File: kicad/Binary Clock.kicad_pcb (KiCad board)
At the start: 2 copper layers, 162.6 x 101.6 mm, 53 parts, among them J1 AVR-ISP-10, SW1 INC_HOUR, SW2 INC_MINUTE, SW3 INC_SECOND, U1 ATmega32A-PU, U2 PCF8583P, Y1 32768hZ

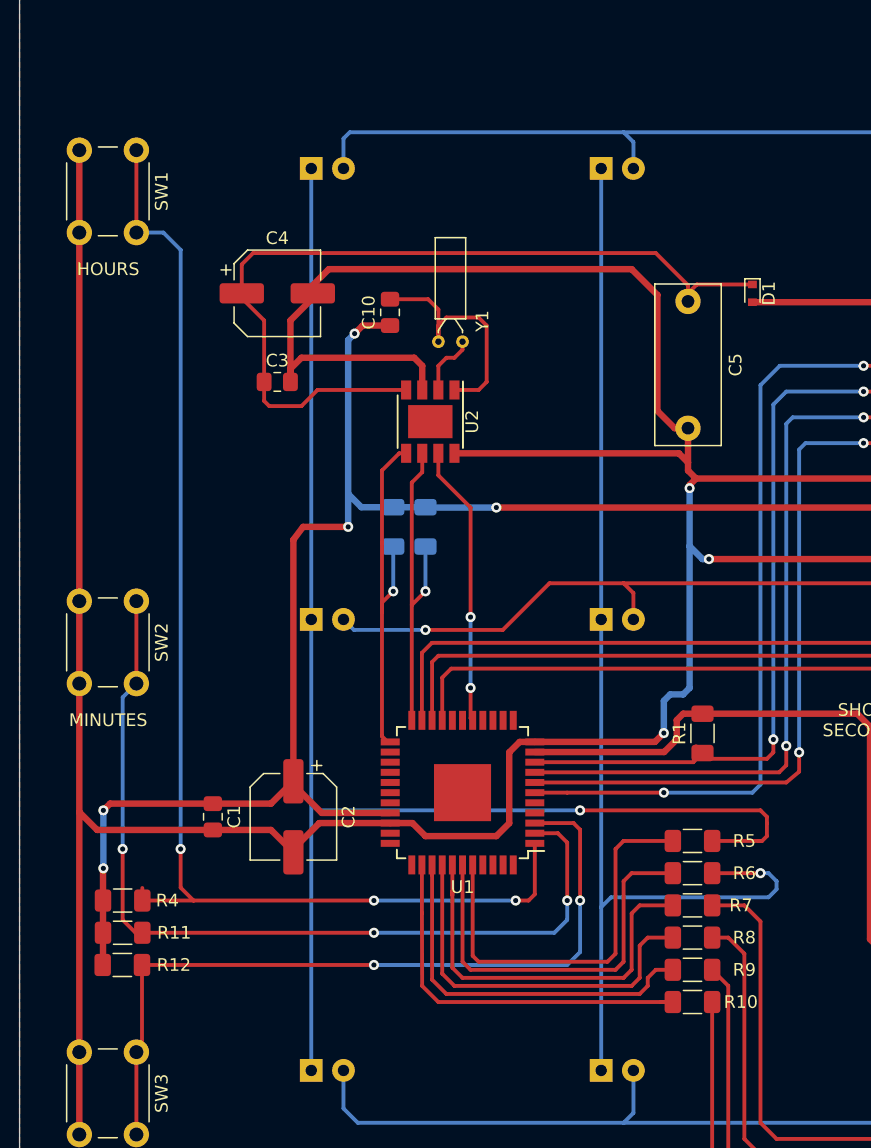
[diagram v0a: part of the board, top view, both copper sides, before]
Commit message: Add INC_BTNESS button to PCB
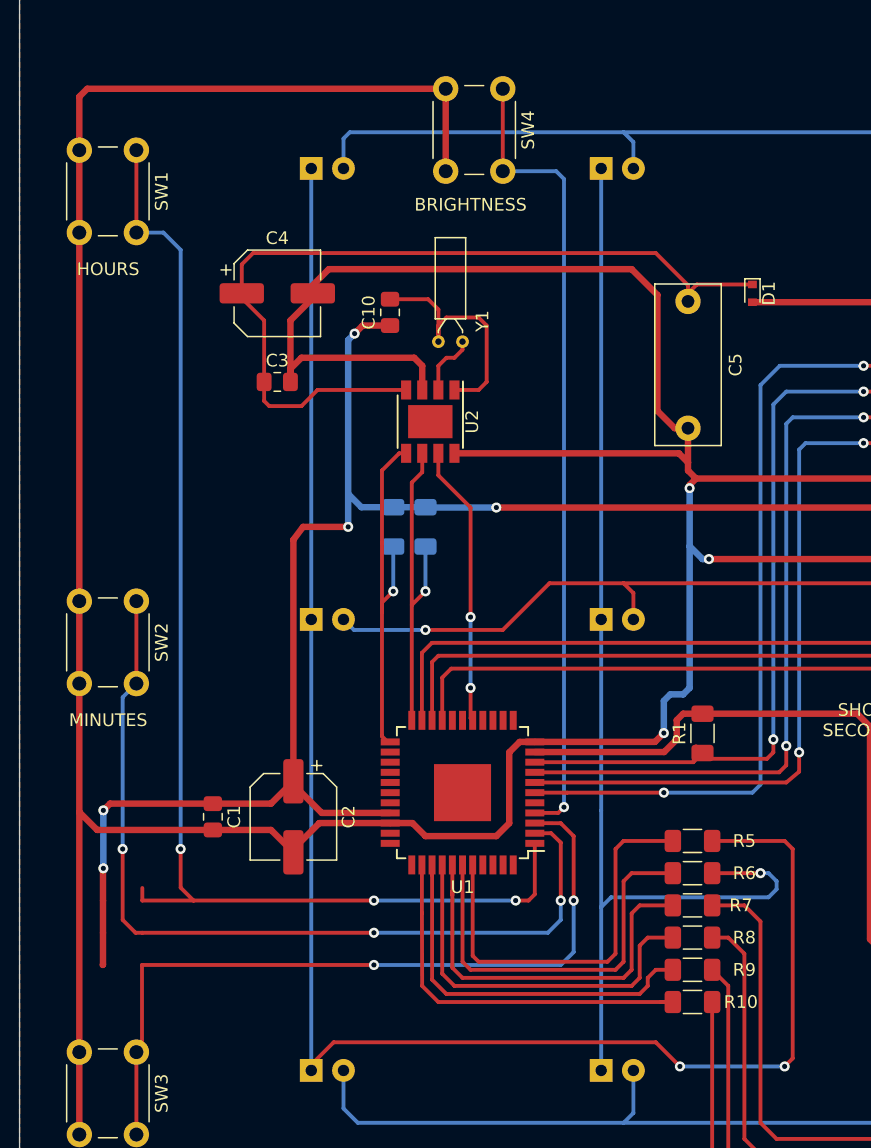
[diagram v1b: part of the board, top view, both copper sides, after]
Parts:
- removed R11, R12, R4: 10k, Resistor_SMD:R_1206_3216Metric_Pad1.30x1.75mm_HandSolder
- added SW4: INC_BTNESS, Button_Switch_THT:SW_PUSH_6mm, F.Cu at (104.1, 64.5)
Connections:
- U1 pad 4: Net-(U1-Pad4) -> /INC_BTNESS
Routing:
- net /INC_BTNESS: track 0.00 -> 63.6 mm, vias 0 -> 1
- net GND: track 424.0 -> 463.9 mm
- net Net-(HD0-Pad1): track 114.2 -> 136.2 mm, vias 1 -> 2
- net /INC_SECOND: track 62.0 -> 60.6 mm
- net /INC_MINUTE: track 70.4 -> 69.4 mm
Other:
- board text added: "BRIGHTNESS"

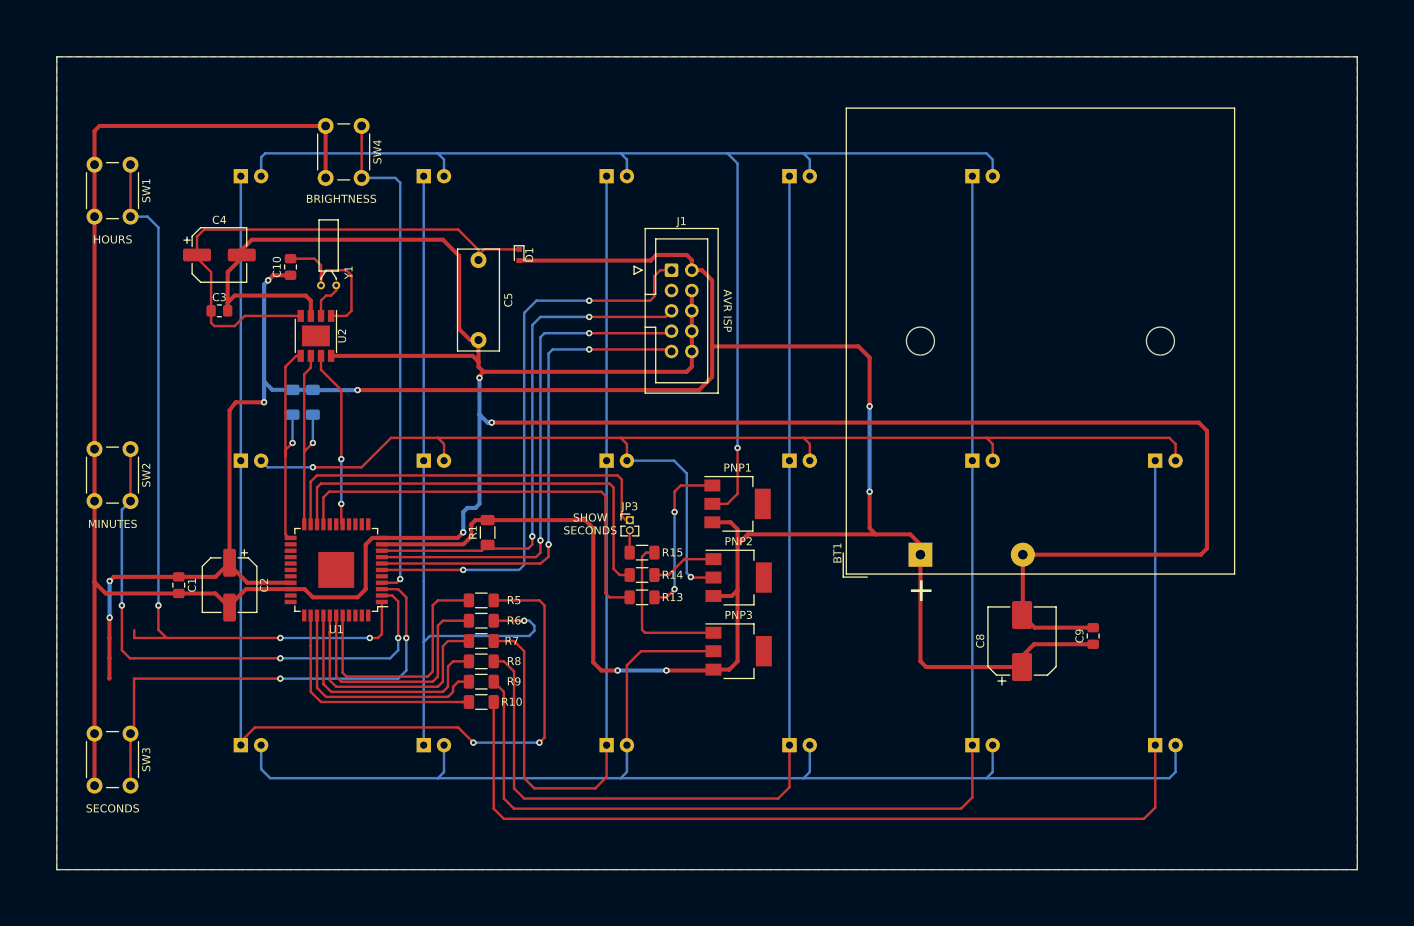
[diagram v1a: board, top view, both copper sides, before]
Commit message: Update schema and PCB design
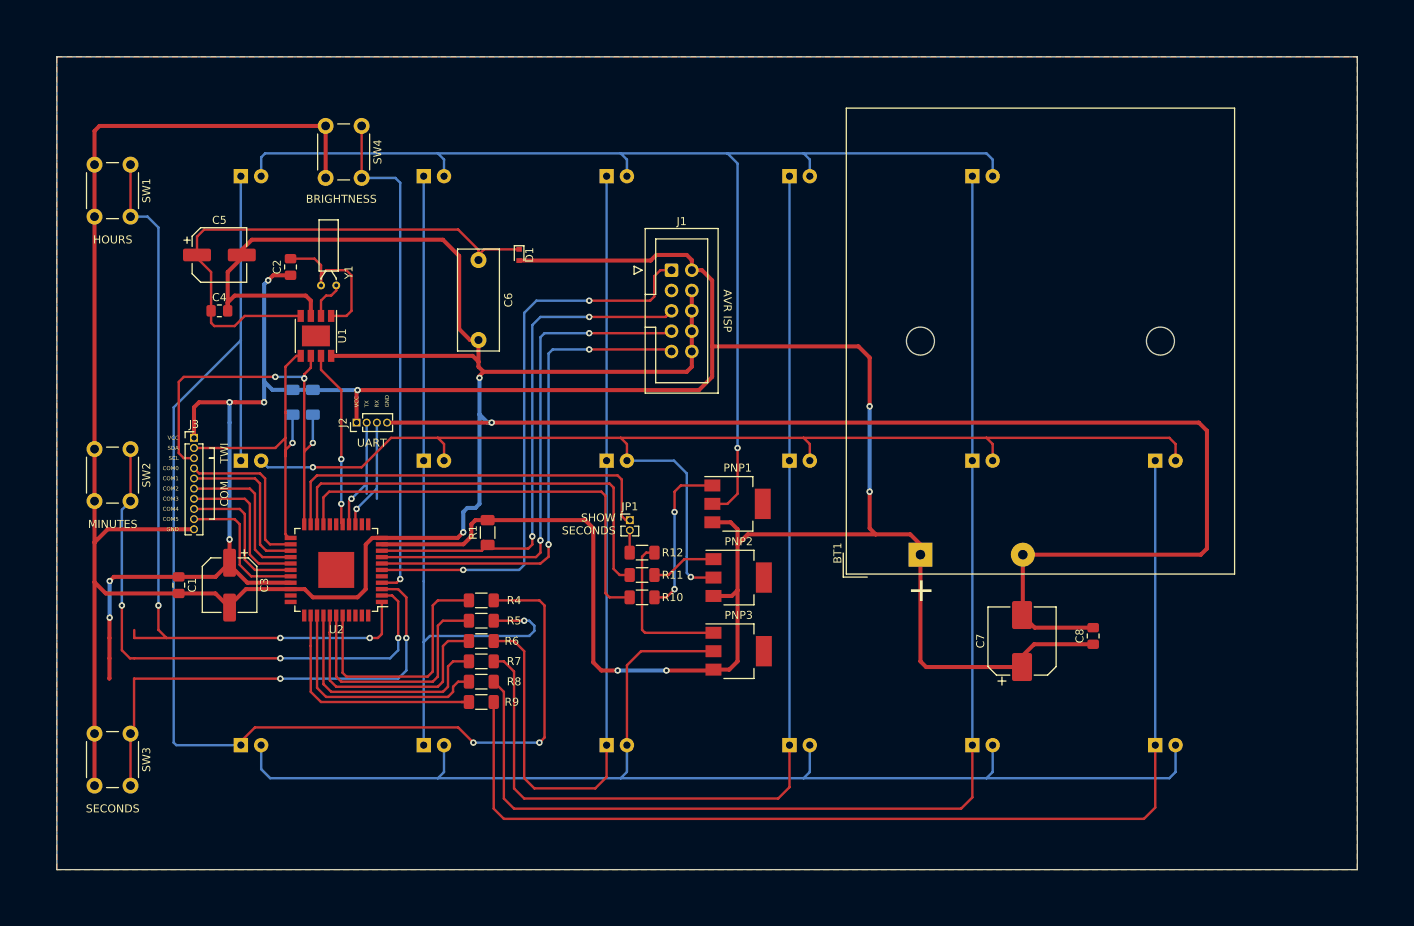
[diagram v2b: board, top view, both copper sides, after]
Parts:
- added J2: UART, Connector_PinHeader_1.27mm:PinHeader_1x04_P1.27mm_Vertical, F.Cu at (103.5, 101.6)
- added J3: COM/TWI, Connector_PinHeader_1.27mm:PinHeader_1x10_P1.27mm_Vertical, F.Cu at (83.2, 103.5)
- renumbered C10 to C2, C2 to C3, C3 to C4, C4 to C5, C5 to C6, C8 to C7, C9 to C8, HD0 to HD1, HD1 to HD2, HD2 to HD3, HD3 to HD4, HD4 to HD5, JP3 to JP1, MD0 to MD1, MD1 to MD2, MD2 to MD3, MD3 to MD4, MD4 to MD5, MD5 to MD6, R13 to R10, R14 to R11, R15 to R12, R5 to R4, R6 to R5, R7 to R6, R8 to R7, R9 to R8, R10 to R9, SD0 to SD1, SD1 to SD2, SD2 to SD3, SD3 to SD4, SD4 to SD5, SD5 to SD6, U2 to U1, U1 to U2
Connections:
- U2 pad 14: Net-(U1-Pad14) -> /RX
- U2 pad 15: Net-(U1-Pad15) -> /TX
- U2 pad 24: Net-(U1-Pad24) -> /COM0
- U2 pad 25: Net-(U1-Pad25) -> /COM1
- U2 pad 26: Net-(U1-Pad26) -> /COM2
- U2 pad 27: Net-(U1-Pad27) -> /COM3
- U2 pad 28: Net-(U1-Pad28) -> /COM4
- U2 pad 29: Net-(U1-Pad29) -> /COM5
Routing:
- net /SCL: track 26.5 -> 53.9 mm, vias 1 -> 3
- net GND: track 463.9 -> 490.1 mm
- net Net-(HD1-Pad1): track 136.2 -> 162.0 mm
- net /COM0: track 0.00 -> 20.5 mm
- net /COM1: track 0.00 -> 20.3 mm
- net /COM2: track 0.00 -> 19.7 mm
- net /COM3: track 0.00 -> 19.2 mm
- net /COM4: track 0.00 -> 18.6 mm
- net /COM5: track 0.00 -> 18.0 mm
- net /RX: track 0.00 -> 15.1 mm, vias 0 -> 1
- net /TX: track 0.00 -> 14.9 mm, vias 0 -> 1
- net VCC: track 368.6 -> 381.7 mm, vias 9 -> 11
- net /SDA: track 29.8 -> 41.8 mm
- net Net-(HD0-Pad1): track 0.00 -> 0.92 mm
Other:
- board text added: "COM"
- board text added: "COM0"
- board text added: "COM1"
- board text added: "COM2"
- board text added: "COM3"
- board text added: "COM4"
- board text added: "COM5"
- board text added: "GND"
- board text added: "RX"
- board text added: "SCL"
- board text added: "SDA"
- board text added: "TWI"
- board text added: "TX"
- board text added: "UART"
- board text added: "VCC"

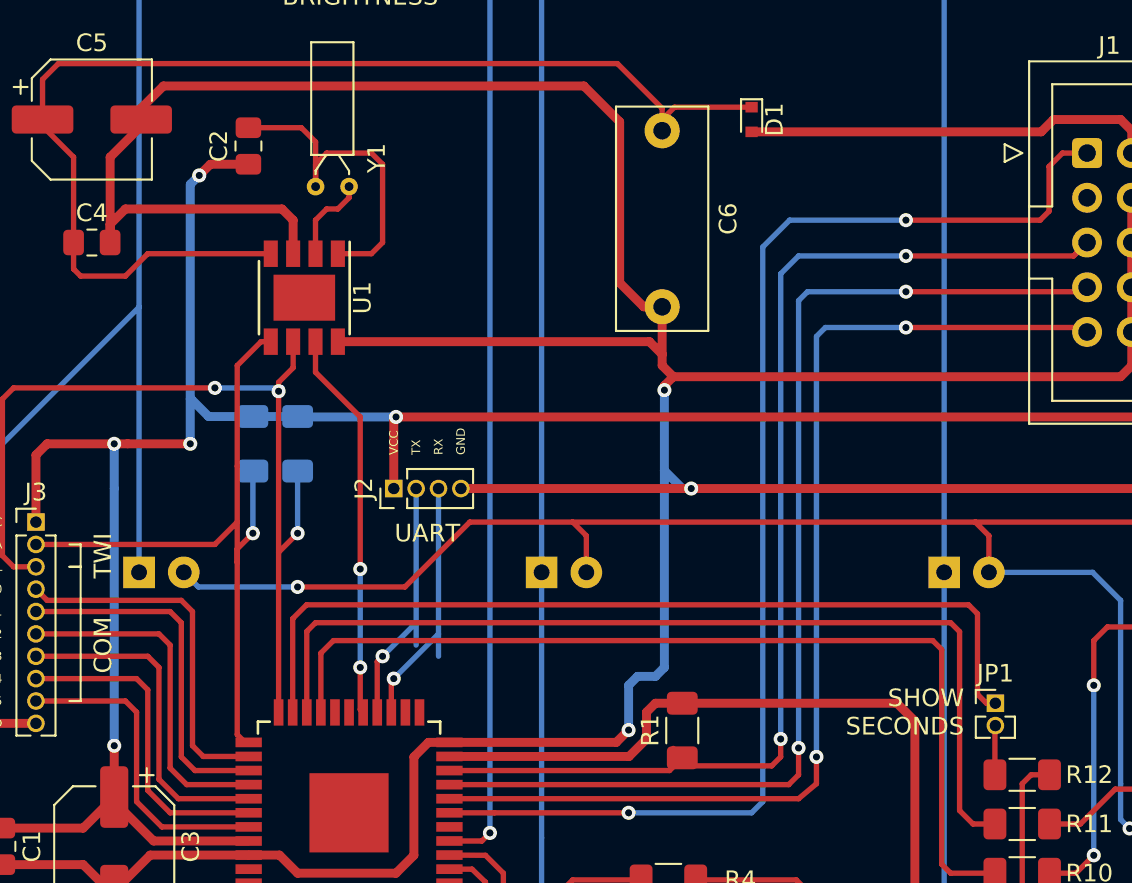
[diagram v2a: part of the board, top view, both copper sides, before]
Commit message: Update schema and PCB design
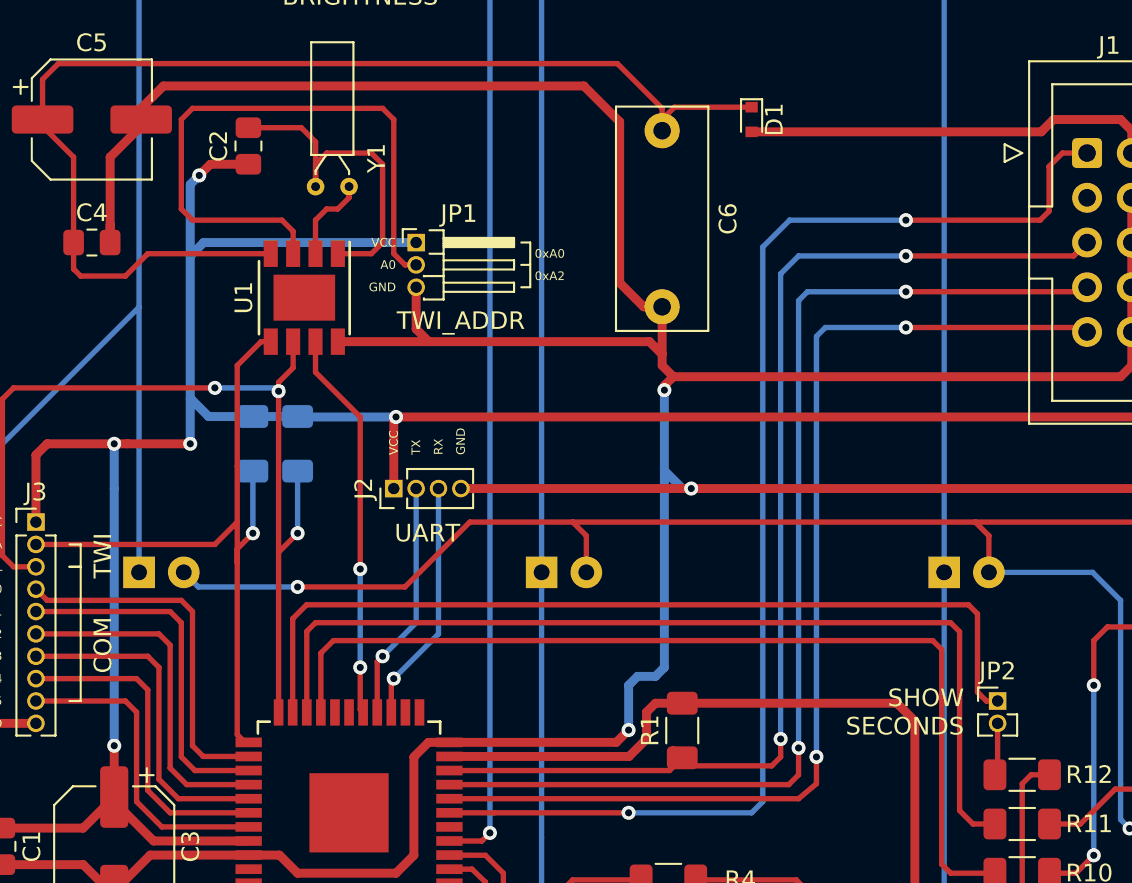
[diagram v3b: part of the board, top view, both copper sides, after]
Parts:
- added JP2: S_EN, Connector_PinHeader_1.27mm:PinHeader_1x02_P1.27mm_Vertical, F.Cu at (137.8, 113.7)
- JP1: value S_EN -> TWI_ADDR; footprint Connector_PinHeader_1.27mm:PinHeader_1x02_P1.27mm_Vertical -> Connector_PinHeader_1.27mm:PinHeader_1x03_P1.27mm_Horizontal
- moved JP1 42.0 mm to (104.8, 87.6)
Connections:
- JP1 pad 1: /SECOND_LED -> VCC
- R12 pad 2: Net-(JP1-Pad2) -> Net-(JP2-Pad2)
- U1 pad 3: GND -> Net-(JP1-Pad2)
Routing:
- net Net-(JP1-Pad2): track 2.80 -> 35.0 mm
- net VCC: track 381.7 -> 394.9 mm
- net GND: track 490.1 -> 480.6 mm
- net Net-(JP2-Pad2): track 0.00 -> 3.02 mm
- net /TX: track 14.9 -> 13.6 mm
- net /RX: track 15.1 -> 13.8 mm
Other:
- board text added: "0xA0"
- board text added: "0xA2"
- board text added: "A0"
- board text added: "TWI_ADDR"
